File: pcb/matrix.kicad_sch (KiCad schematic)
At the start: 134 parts

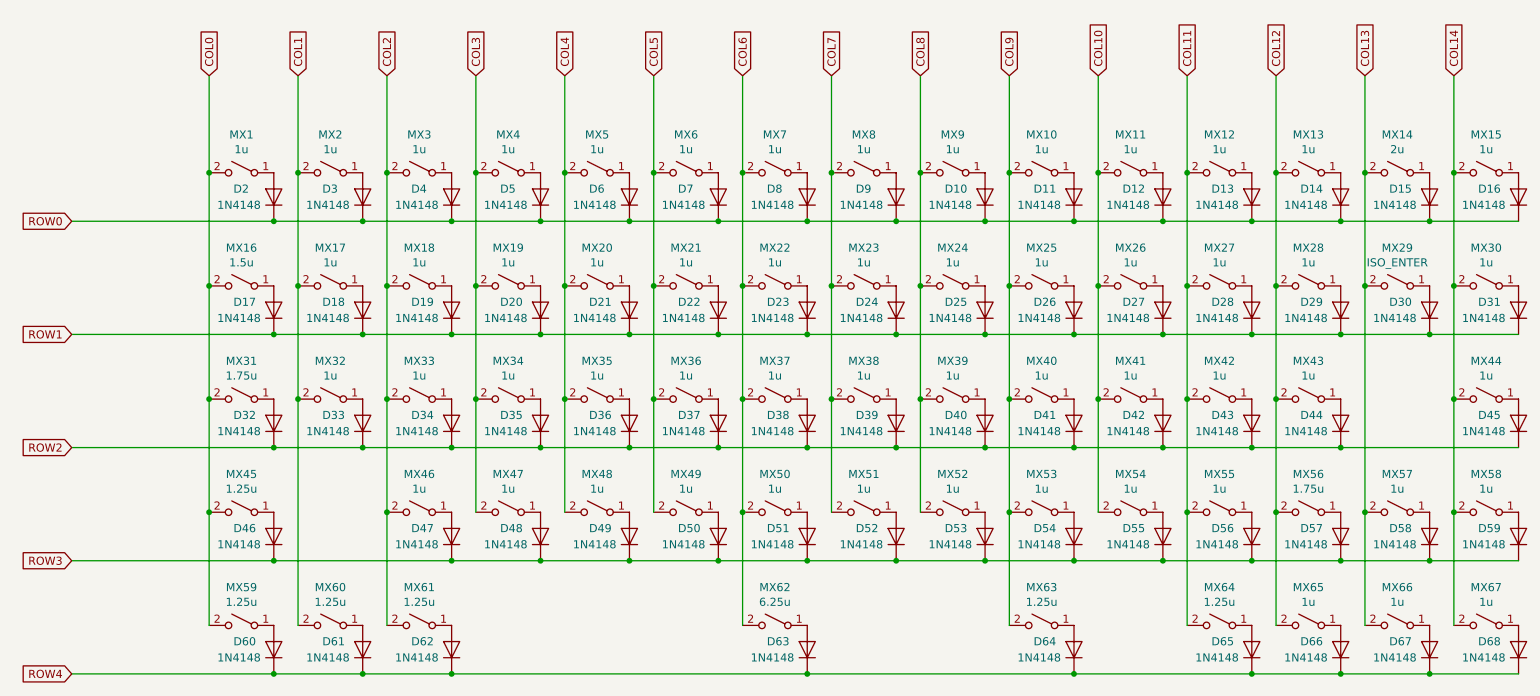
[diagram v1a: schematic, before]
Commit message: 🧹Cleaned more up and updated the readme
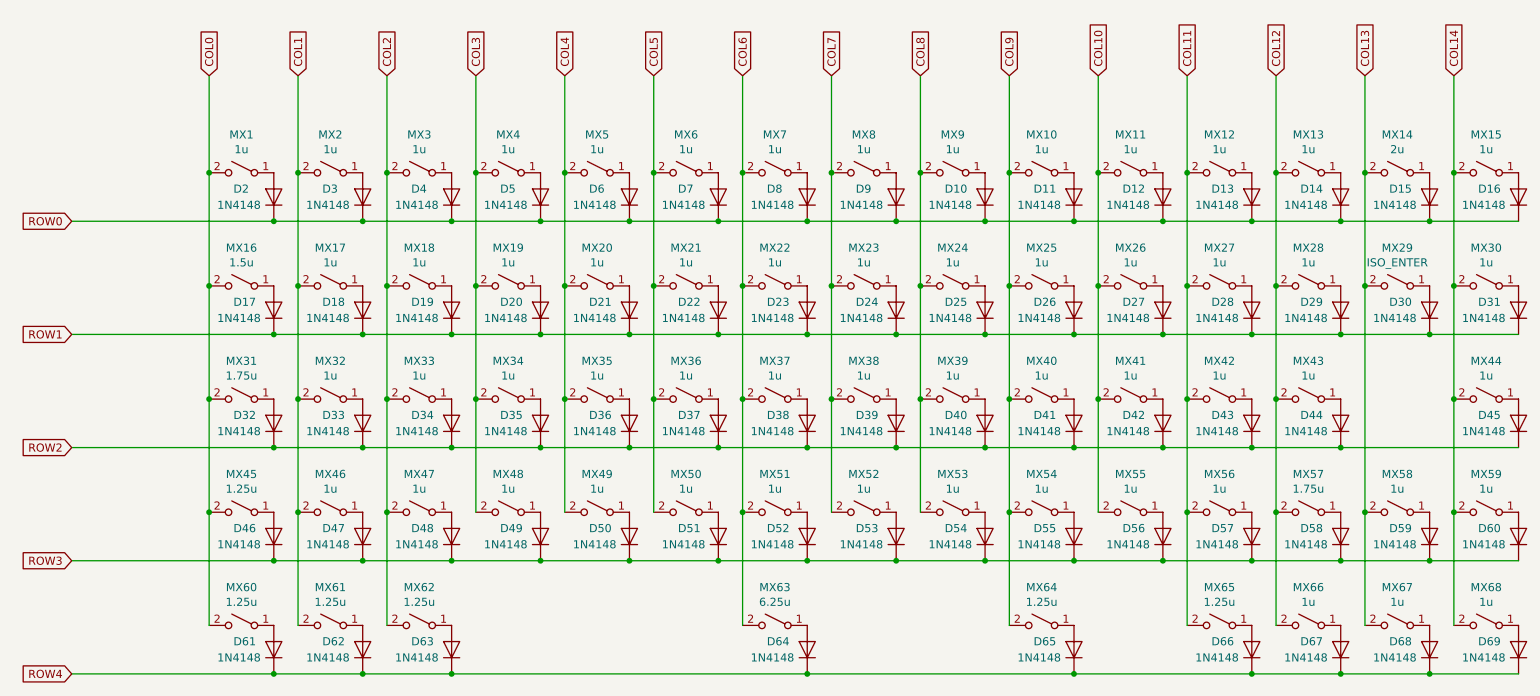
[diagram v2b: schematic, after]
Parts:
- added D47: 1N4148, Diode_SMD:D_SOD-123, symbol Device:D
- added MX46: 1u, PCM_marbastlib-mx:SW_MX_1u, symbol Switch:SW_SPST
- MX1, MX10, MX11, MX12, MX13, MX15, MX17, MX18, MX19, MX2, MX20, MX21, MX22, MX23, MX24, MX25, MX26, MX27, MX28, MX3, MX30, MX32, MX33, MX34, MX35, MX36, MX37, MX38, MX39, MX4, MX40, MX41, MX42, MX43, MX44, MX5, MX6, MX7, MX8, MX9: footprint MX_Only:MXOnly-1U-NoLED -> PCM_marbastlib-mx:SW_MX_1u; now left out of the parts list
- MX14: footprint MX_Only:MXOnly-2U-NoLED -> PCM_marbastlib-mx:SW_MX_1u; now left out of the parts list
- MX16: footprint MX_Only:MXOnly-1.5U-NoLED -> PCM_marbastlib-mx:SW_MX_1.5u; now left out of the parts list
- MX29: footprint MX_Only:MXOnly-ISO-ROTATED-ReversedStabilizers-NoLED -> PCM_marbastlib-mx:SW_MX_1u; now left out of the parts list
- MX31: footprint MX_Only:MXOnly-1.75U-NoLED -> PCM_marbastlib-mx:SW_MX_1.75u; now left out of the parts list
- MX45: footprint MX_Only:MXOnly-2.25U-NoLED -> PCM_marbastlib-mx:SW_MX_1.25u; now left out of the parts list
- MX47: renamed from MX46; footprint MX_Only:MXOnly-1U-NoLED -> PCM_marbastlib-mx:SW_MX_1u; now left out of the parts list
- MX48: renamed from MX47; footprint MX_Only:MXOnly-1U-NoLED -> PCM_marbastlib-mx:SW_MX_1u; now left out of the parts list
- MX49: renamed from MX48; footprint MX_Only:MXOnly-1U-NoLED -> PCM_marbastlib-mx:SW_MX_1u; now left out of the parts list
- MX50: renamed from MX49; footprint MX_Only:MXOnly-1U-NoLED -> PCM_marbastlib-mx:SW_MX_1u; now left out of the parts list
- MX51: renamed from MX50; footprint MX_Only:MXOnly-1U-NoLED -> PCM_marbastlib-mx:SW_MX_1u; now left out of the parts list
- MX52: renamed from MX51; footprint MX_Only:MXOnly-1U-NoLED -> PCM_marbastlib-mx:SW_MX_1u; now left out of the parts list
- MX53: renamed from MX52; footprint MX_Only:MXOnly-1U-NoLED -> PCM_marbastlib-mx:SW_MX_1u; now left out of the parts list
- MX54: renamed from MX53; footprint MX_Only:MXOnly-1U-NoLED -> PCM_marbastlib-mx:SW_MX_1u; now left out of the parts list
- MX55: renamed from MX54; footprint MX_Only:MXOnly-1U-NoLED -> PCM_marbastlib-mx:SW_MX_1u; now left out of the parts list
- MX56: renamed from MX55; footprint MX_Only:MXOnly-1U-NoLED -> PCM_marbastlib-mx:SW_MX_1u; now left out of the parts list
- MX57: renamed from MX56; footprint MX_Only:MXOnly-1.75U-NoLED -> PCM_marbastlib-mx:SW_MX_1.75u; now left out of the parts list
- MX58: renamed from MX57; footprint MX_Only:MXOnly-1U-NoLED -> PCM_marbastlib-mx:SW_MX_1u; now left out of the parts list
- MX59: renamed from MX58; footprint MX_Only:MXOnly-1U-NoLED -> PCM_marbastlib-mx:SW_MX_1u; now left out of the parts list
- MX60: renamed from MX59; footprint MX_Only:MXOnly-1.25U-NoLED -> PCM_marbastlib-mx:SW_MX_1.25u; now left out of the parts list
- MX61: renamed from MX60; footprint MX_Only:MXOnly-1.25U-NoLED -> PCM_marbastlib-mx:SW_MX_1.25u; now left out of the parts list
- MX62: renamed from MX61; footprint MX_Only:MXOnly-1.25U-NoLED -> PCM_marbastlib-mx:SW_MX_1.25u; now left out of the parts list
- MX63: renamed from MX62; footprint MX_Only:MXOnly-6.25U-ReversedStabilizers-NoLED -> PCM_marbastlib-mx:SW_MX_1u; now left out of the parts list
- MX64: renamed from MX63; footprint MX_Only:MXOnly-1.25U-NoLED -> PCM_marbastlib-mx:SW_MX_1.25u; now left out of the parts list
- MX65: renamed from MX64; footprint MX_Only:MXOnly-1.25U-NoLED -> PCM_marbastlib-mx:SW_MX_1.25u; now left out of the parts list
- MX66: renamed from MX65; footprint MX_Only:MXOnly-1U-NoLED -> PCM_marbastlib-mx:SW_MX_1u; now left out of the parts list
- MX67: renamed from MX66; footprint MX_Only:MXOnly-1U-NoLED -> PCM_marbastlib-mx:SW_MX_1u; now left out of the parts list
- MX68: renamed from MX67; footprint MX_Only:MXOnly-1U-NoLED -> PCM_marbastlib-mx:SW_MX_1u; now left out of the parts list
- renumbered D47 to D48, D48 to D49, D49 to D50, D50 to D51, D51 to D52, D52 to D53, D53 to D54, D54 to D55, D55 to D56, D56 to D57, D57 to D58, D58 to D59, D59 to D60, D60 to D61, D61 to D62, D62 to D63, D63 to D64, D64 to D65, D65 to D66, D66 to D67, D67 to D68, D68 to D69
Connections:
- net COL1: now also MX46.2 (B)
- net ROW3: now also D47.1 (K)
- new net: D47.2 (A), MX46.1 (A)
